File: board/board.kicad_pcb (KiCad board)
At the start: 2 copper layers, 50.8 x 22.9 mm, 17 parts, among them J1 MOTION DETECTOR, J2 EXT BUTTON, J3 GS2, J4 ~POWER, U3 ATTINY85

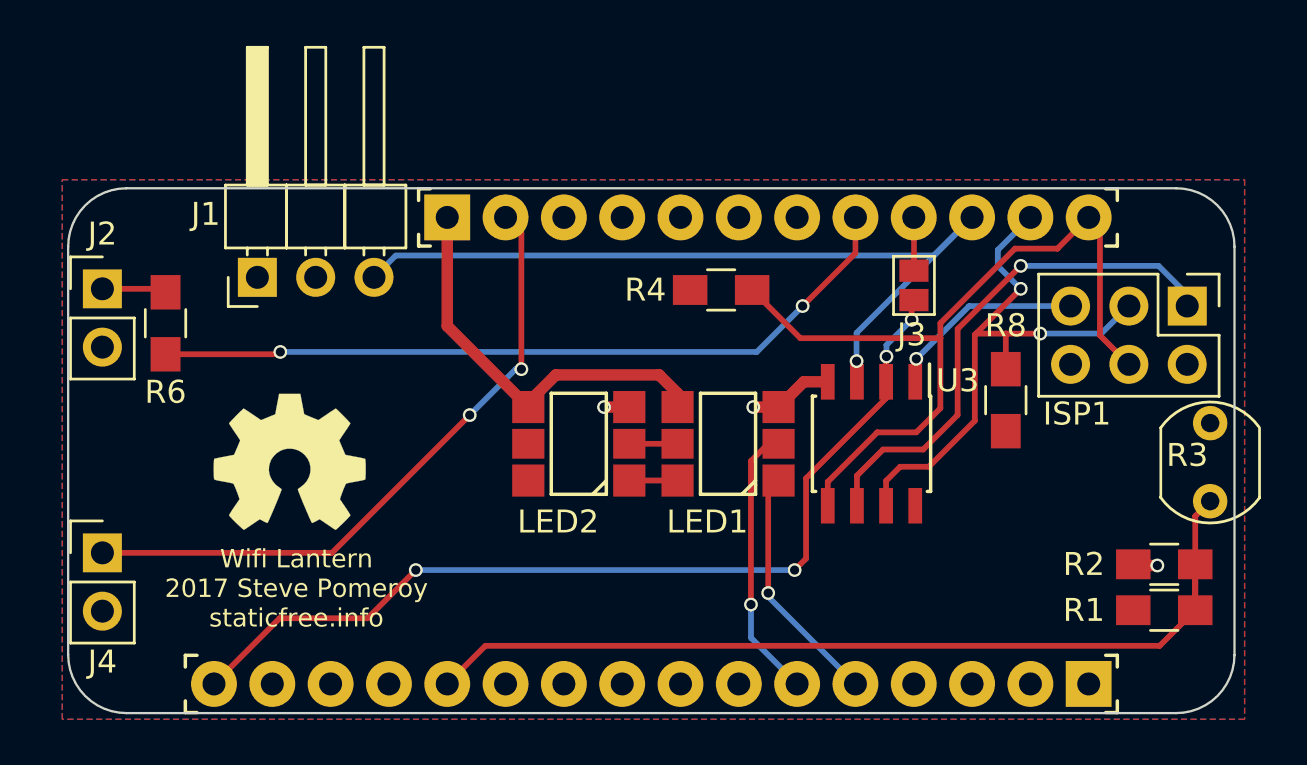
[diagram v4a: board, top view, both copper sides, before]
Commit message: Add power breakout; updated on-board docs
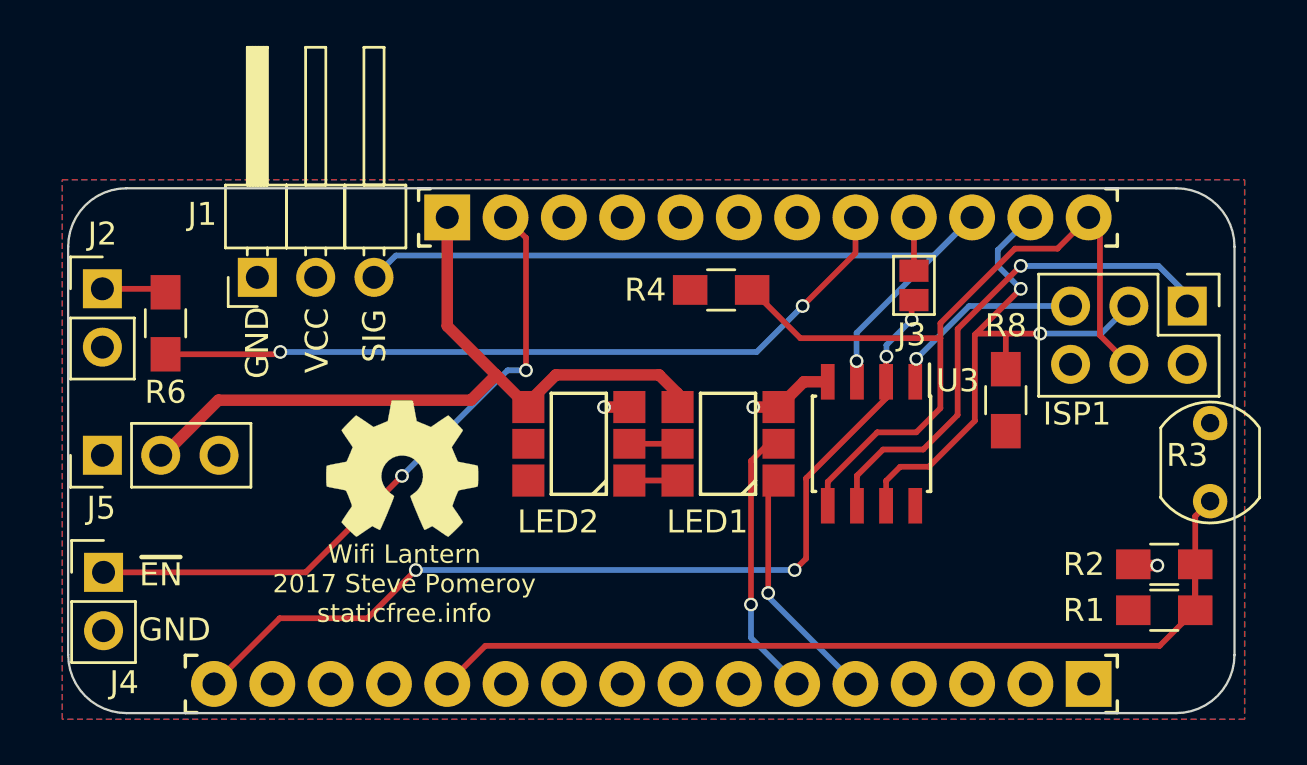
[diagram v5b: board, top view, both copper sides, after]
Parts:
- added J5: GPWR, Pin_Headers:Pin_Header_Straight_1x03_Pitch2.54mm, F.Cu at (113.2, 114.5)
- U3: value ATTINY85 -> ATTINY85-20PU
- moved REF*** 4.91 mm to (126.3, 115.1)
- moved J4 0.85 mm to (113.3, 119.6)
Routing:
- net /VBAT: track 18.1 -> 34.1 mm
- net /EN: track 28.5 -> 29.1 mm
- net Net-(ISP1-Pad5): vias 2 -> 1
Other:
- board text added: "EXT BTN (D9)"
- board text added: "GND"
- board text added: "J3: short for ESP8266 built-in RTC reset"
- board text added: "Power"
- board text added: "SIG"
- board text added: "VBAT"
- board text added: "VCC"
- board text added: "~EN"
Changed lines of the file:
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@@
 (kicad_pcb (version 4) (host pcbnew 4.0.6+dfsg1-1)
   (general
-    (links 40)
+    (links 43)
     (no_connects 0)
     (area 111.709999 102.819999 162.610001 125.780001)
     (thickness 1.6)
-    (drawings 9)
-    (tracks 140)
+    (drawings 20)
+    (tracks 144)
     (zones 0)
-    (modules 17)
+    (modules 18)
     (nets 19)
   )
@@
   )
   (module Pin_Headers:Pin_Header_Straight_1x02_Pitch2.54mm (layer F.Cu)
-    (at 113.25 118.75)
+    (at 113.3 119.6)
     (descr "Through hole straight pin header, 1x02, 2.54mm pitch, single row")
     (tags "Through hole pin header THT 1x02 2.54mm single row")
-    (fp_text reference J4 (at 0 4.75) (layer F.SilkS)
+    (fp_text reference J4 (at 0.9 4.8) (layer F.SilkS)
       (effects (font (size 1 1) (thickness 0.15)))
     )
@@
       (effects (font (size 1 1) (thickness 0.15)))
     )
-    (fp_text value ATTINY85 (at 3 0 360) (layer F.Fab)
+    (fp_text value ATTINY85-20PU (at 3 0 360) (layer F.Fab)
       (effects (font (size 1 1) (thickness 0.15)))
     )
@@
     (descr "Through hole angled pin header, 1x03, 2.54mm pitch, 6mm pin length, single row")
     (tags "Through hole angled pin header THT 1x03 2.54mm single row")
-    (fp_text reference J1 (at 2.75 -2.25 180) (layer F.SilkS)
+    (fp_text reference J1 (at 2.75 -2.4 180) (layer F.SilkS)
       (effects (font (size 1 1) (thickness 0.15)))
     )
@@
   )
   (module Symbols:OSHW-Symbol_6.7x6mm_SilkScreen (layer F.Cu)
-    (at 121.4 114.8)
+    (at 126.3 115.1)
     (descr "Open Source Hardware Symbol")
     (tags "Logo Symbol OSHW")
@@
       (xy 0.555814 -2.531069)) (layer F.SilkS) (width 0.01))
   )
-  (gr_text "Wifi Lantern\n2017 Steve Pomeroy\nstaticfree.info" (at 121.7 120.3) (layer F.SilkS)
+  (module Pin_Headers:Pin_Header_Straight_1x03_Pitch2.54mm (layer F.Cu)
+    (at 113.25 114.5 90)
+    (descr "Through hole straight pin header, 1x03, 2.54mm pitch, single row")
+    (tags "Through hole pin header THT 1x03 2.54mm single row")
+    (fp_text reference J5 (at -2.3 -0.05 180) (layer F.SilkS)
+      (effects (font (size 1 1) (thickness 0.15)))
+    )
+    (fp_text value GPWR (at 0 7.47 90) (layer F.Fab)
+      (effects (font (size 1 1) (thickness 0.15)))
+    )
+    (fp_line (start -1.27 -1.27) (end -1.27 6.35) (layer F.Fab) (width 0.1))
+    (fp_line (start -1.27 6.35) (end 1.27 6.35) (layer F.Fab) (width 0.1))
+    (fp_line (start 1.27 6.35) (end 1.27 -1.27) (layer F.Fab) (width 0.1))
+    (fp_line (start 1.27 -1.27) (end -1.27 -1.27) (layer F.Fab) (width 0.1))
+    (fp_line (start -1.39 1.27) (end -1.39 6.47) (layer F.SilkS) (width 0.12))
+    (fp_line (start -1.39 6.47) (end 1.39 6.47) (layer F.SilkS) (width 0.12))
+    (fp_line (start 1.39 6.47) (end 1.39 1.27) (layer F.SilkS) (width 0.12))
+    (fp_line (start 1.39 1.27) (end -1.39 1.27) (layer F.SilkS) (width 0.12))
+    (fp_line (start -1.39 0) (end -1.39 -1.39) (layer F.SilkS) (width 0.12))
+    (fp_line (start -1.39 -1.39) (end 0 -1.39) (layer F.SilkS) (width 0.12))
+    (fp_line (start -1.6 -1.6) (end -1.6 6.6) (layer F.CrtYd) (width 0.05))
+    (fp_line (start -1.6 6.6) (end 1.6 6.6) (layer F.CrtYd) (width 0.05))
+    (fp_line (start 1.6 6.6) (end 1.6 -1.6) (layer F.CrtYd) (width 0.05))
+    (fp_line (start 1.6 -1.6) (end -1.6 -1.6) (layer F.CrtYd) (width 0.05))
+    (pad 1 thru_hole rect (at 0 0 90) (size 1.7 1.7) (drill 1) (layers *.Cu *.Mask)
+      (net 5 VCC))
+    (pad 2 thru_hole oval (at 0 2.54 90) (size 1.7 1.7) (drill 1) (layers *.Cu *.Mask)
+      (net 4 /VBAT))
+    (pad 3 thru_hole oval (at 0 5.08 90) (size 1.7 1.7) (drill 1) (layers *.Cu *.Mask)
+      (net 3 GND))
+    (model Pin_Headers.3dshapes/Pin_Header_Straight_1x03_Pitch2.54mm.wrl
+      (at (xyz 0 -0.1 0))
+      (scale (xyz 1 1 1))
+      (rotate (xyz 0 0 90))
+    )
+  )
+  (gr_text VBAT (at 115.9 117.5 270) (layer B.SilkS)
+    (effects (font (size 1 1) (thickness 0.2)) (justify mirror))
+  )
+  (gr_text VCC (at 113.4 117.2 270) (layer B.SilkS)
+    (effects (font (size 1 1) (thickness 0.2)) (justify mirror))
+  )
+  (gr_text GND (at 118.4 117.4 270) (layer B.SilkS)
+    (effects (font (size 1 1) (thickness 0.2)) (justify mirror))
+  )
+  (gr_text Power (at 115.4 122 270) (layer B.SilkS)
+    (effects (font (size 0.7 0.7) (thickness 0.1)) (justify mirror))
+  )
+  (gr_text GND (at 116.4 122.1) (layer F.SilkS)
+    (effects (font (size 1 1) (thickness 0.2)))
+  )
+  (gr_text ~EN (at 115.8 119.7) (layer F.SilkS)
+    (effects (font (size 1 1) (thickness 0.2)))
+  )
+  (gr_text "EXT BTN (D9)" (at 115.2 108.5 270) (layer B.SilkS)
+    (effects (font (size 0.7 0.7) (thickness 0.1)) (justify mirror))
+  )
+  (gr_text SIG (at 125.1 109.3 90) (layer F.SilkS)
+    (effects (font (size 1 1) (thickness 0.2)))
+  )
+  (gr_text VCC (at 122.6 109.5 90) (layer F.SilkS)
+    (effects (font (size 1 1) (thickness 0.2)))
+  )
+  (gr_text GND (at 120 109.6 90) (layer F.SilkS)
+    (effects (font (size 1 1) (thickness 0.2)))
+  )
+  (gr_text "J3: short for\nESP8266 built-in RTC reset" (at 145.7 113.3) (layer B.SilkS)
+    (effects (font (size 0.7 0.7) (thickness 0.1)) (justify mirror))
+  )
+  (gr_text "Wifi Lantern\n2017 Steve Pomeroy\nstaticfree.info" (at 126.4 120.1) (layer F.SilkS)
     (effects (font (size 0.8 0.8) (thickness 0.1)))
   )
@@
   (segment (start 143.8 111.3) (end 144.845 111.3) (width 0.5) (layer F.Cu) (net 3) (status 20))
   (segment (start 136.2 112.4) (end 136.1 112.5) (width 0.5) (layer F.Cu) (net 3) (status 30))
+  (segment (start 115.79 114.5) (end 115.9 114.5) (width 0.5) (layer F.Cu) (net 4) (status 30))
+  (segment (start 115.9 114.5) (end 118.3 112.1) (width 0.5) (layer F.Cu) (net 4) (status 10))
+  (segment (start 118.3 112.1) (end 129.3 112.1) (width 0.5) (layer F.Cu) (net 4))
+  (segment (start 129.3 112.1) (end 130.4 111) (width 0.5) (layer F.Cu) (net 4))
   (segment (start 138.3 112.4) (end 138.3 112.2) (width 0.5) (layer F.Cu) (net 4) (status 30))
   (segment (start 131.8 112.4) (end 131.8 112.2) (width 0.5) (layer F.Cu) (net 4) (status 30))
@@
   (segment (start 133 111) (end 137.5 111) (width 0.5) (layer F.Cu) (net 4))
   (segment (start 138.3 111.8) (end 138.3 112.4) (width 0.5) (layer F.Cu) (net 4) (status 30))
-  (segment (start 131.8 112.4) (end 128.27 108.87) (width 0.5) (layer F.Cu) (net 4) (status 10))
+  (segment (start 131.8 112.4) (end 130.4 111) (width 0.5) (layer F.Cu) (net 4) (status 10))
+  (segment (start 130.4 111) (end 128.27 108.87) (width 0.5) (layer F.Cu) (net 4))
   (segment (start 128.27 108.87) (end 128.27 104.14) (width 0.5) (layer F.Cu) (net 4) (status 20))
   (segment (start 120.65 124.35) (end 120.65 124.46) (width 0.5) (layer F.Cu) (net 5) (status 30))
@@
   (via (at 148.7 110.3) (size 0.6) (drill 0.4) (layers F.Cu B.Cu) (net 10))
   (segment (start 151 108) (end 148.7 110.3) (width 0.25) (layer B.Cu) (net 10))
-  (via (at 155.42 108) (size 0.6) (drill 0.4) (layers F.Cu B.Cu) (net 10) (status 30))
   (segment (start 148.7 111.255) (end 148.655 111.3) (width 0.25) (layer F.Cu) (net 10) (status 30))
   (segment (start 116 107.4) (end 115.85 107.25) (width 0.25) (layer F.Cu) (net 11) (status 30))
@@
   (segment (start 148 115) (end 149.25 115) (width 0.25) (layer F.Cu) (net 15))
   (segment (start 147.385 115.615) (end 148 115) (width 0.25) (layer F.Cu) (net 15))
-  (segment (start 144.845 116.7) (end 144.845 115.655) (width 0.25) (layer F.Cu) (net 16))
+  (segment (start 144.845 116.7) (end 144.845 115.655) (width 0.25) (layer F.Cu) (net 16) (status 10))
   (segment (start 149.75 112.45) (end 149.75 109.4) (width 0.25) (layer F.Cu) (net 16))
   (segment (start 148.7 113.5) (end 149.75 112.45) (width 0.25) (layer F.Cu) (net 16))
@@
   (segment (start 149.75 108.75) (end 153 105.5) (width 0.25) (layer F.Cu) (net 16))
   (segment (start 149.75 109.4) (end 149.75 108.75) (width 0.25) (layer F.Cu) (net 16))
-  (segment (start 113.25 118.75) (end 123.25 118.75) (width 0.25) (layer F.Cu) (net 17) (status 10))
-  (segment (start 131.5 110.75) (end 131.5 104.83) (width 0.25) (layer F.Cu) (net 17) (status 20))
-  (via (at 131.5 110.75) (size 0.6) (drill 0.4) (layers F.Cu B.Cu) (net 17))
-  (segment (start 131.25 110.75) (end 131.5 110.75) (width 0.25) (layer B.Cu) (net 17))
-  (segment (start 129.25 112.75) (end 131.25 110.75) (width 0.25) (layer B.Cu) (net 17))
-  (via (at 129.25 112.75) (size 0.6) (drill 0.4) (layers F.Cu B.Cu) (net 17))
-  (segment (start 123.25 118.75) (end 129.25 112.75) (width 0.25) (layer F.Cu) (net 17))
-  (segment (start 131.5 104.83) (end 130.81 104.14) (width 0.25) (layer F.Cu) (net 17) (status 30))
+  (segment (start 113.3 119.6) (end 122.1 119.6) (width 0.25) (layer F.Cu) (net 17) (status 10))
+  (segment (start 131.7 105.03) (end 130.81 104.14) (width 0.25) (layer F.Cu) (net 17) (status 20))
+  (segment (start 131.7 110.8) (end 131.7 105.03) (width 0.25) (layer F.Cu) (net 17))
+  (via (at 131.7 110.8) (size 0.6) (drill 0.4) (layers F.Cu B.Cu) (net 17))
+  (segment (start 130.9 110.8) (end 131.7 110.8) (width 0.25) (layer B.Cu) (net 17))
+  (segment (start 126.3 115.4) (end 130.9 110.8) (width 0.25) (layer B.Cu) (net 17))
+  (via (at 126.3 115.4) (size 0.6) (drill 0.4) (layers F.Cu B.Cu) (net 17))
+  (segment (start 122.1 119.6) (end 126.3 115.4) (width 0.25) (layer F.Cu) (net 17))
   (segment (start 116 110.1) (end 120.9 110.1) (width 0.25) (layer F.Cu) (net 18) (status 10))
   (segment (start 146.05 105.7) (end 146.05 104.14) (width 0.25) (layer F.Cu) (net 18) (status 20))

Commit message: Improve on-board docs
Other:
- board text added: "EXT BTN"
- board text added: "Wifi Lantern v0.5.0 2017 Steve Pomeroy staticfree.info"
- board text added: "~Power"
- board text removed: "EXT BTN (D9)"
- board text removed: "Power"
- board text removed: "Wifi Lantern 2017 Steve Pomeroy staticfree.info"
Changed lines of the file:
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@@
     (descr "Through hole straight pin header, 1x02, 2.54mm pitch, single row")
     (tags "Through hole pin header THT 1x02 2.54mm single row")
-    (fp_text reference J4 (at 0.9 4.8) (layer F.SilkS)
-      (effects (font (size 1 1) (thickness 0.15)))
+    (fp_text reference J4 (at 0.9 4.8) (layer B.SilkS)
+      (effects (font (size 1 1) (thickness 0.15)) (justify mirror))
     )
     (fp_text value ~POWER (at -4.5 1 180) (layer F.Fab)
@@
     (tags "solder bridge")
     (attr smd)
-    (fp_text reference J3 (at -0.1 2.15 180) (layer F.SilkS)
+    (fp_text reference J3 (at -2 -0.7 180) (layer F.SilkS)
       (effects (font (size 1 1) (thickness 0.15)))
     )
@@
     (tags "resistor 0805")
     (attr smd)
-    (fp_text reference R8 (at 3.25 0 180) (layer F.SilkS)
+    (fp_text reference R8 (at 3 0 180) (layer F.SilkS)
       (effects (font (size 1 1) (thickness 0.15)))
     )
@@
       (effects (font (size 1 1) (thickness 0.15)))
     )
-    (fp_text user %R (at 3.25 0 180) (layer F.Fab)
+    (fp_text user %R (at 3 0 180) (layer F.Fab)
       (effects (font (size 1 1) (thickness 0.15)))
     )
@@
       (effects (font (size 1 1) (thickness 0.15)))
     )
-    (fp_text user %R (at -3.2 0 180) (layer F.Fab)
+    (fp_text user %R (at -3.3 0 180) (layer F.Fab)
       (effects (font (size 1 1) (thickness 0.15)))
     )
@@
     (descr "Through hole straight pin header, 1x02, 2.54mm pitch, single row")
     (tags "Through hole pin header THT 1x02 2.54mm single row")
-    (fp_text reference J2 (at 0 -2.39) (layer F.SilkS)
-      (effects (font (size 1 1) (thickness 0.15)))
+    (fp_text reference J2 (at 0 -2.39) (layer B.SilkS)
+      (effects (font (size 1 1) (thickness 0.15)) (justify mirror))
     )
     (fp_text value "EXT BUTTON" (at -6.25 1.5) (layer F.Fab)
@@
     (tags "SOIC 1.27")
     (attr smd)
-    (fp_text reference U3 (at -2.75 -3.75 360) (layer F.SilkS)
+    (fp_text reference U3 (at -4.3 1.75 360) (layer F.SilkS)
       (effects (font (size 1 1) (thickness 0.15)))
     )
@@
     (descr "Resistor, LDR 5.1x3.4mm")
     (tags "Resistor LDR5.1x3.4mm")
-    (fp_text reference R3 (at 2 -1 180) (layer F.SilkS)
+    (fp_text reference R3 (at 1.7 -1 180) (layer F.SilkS)
       (effects (font (size 1 1) (thickness 0.15)))
     )
@@
     (descr "Through hole straight pin header, 1x03, 2.54mm pitch, single row")
     (tags "Through hole pin header THT 1x03 2.54mm single row")
-    (fp_text reference J5 (at -2.3 -0.05 180) (layer F.SilkS)
-      (effects (font (size 1 1) (thickness 0.15)))
+    (fp_text reference J5 (at -2.3 -0.05 180) (layer B.SilkS)
+      (effects (font (size 1 1) (thickness 0.15)) (justify mirror))
     )
     (fp_text value GPWR (at 0 7.47 90) (layer F.Fab)
@@
     )
   )
-  (gr_text VBAT (at 115.9 117.5 270) (layer B.SilkS)
-    (effects (font (size 1 1) (thickness 0.2)) (justify mirror))
-  )
-  (gr_text VCC (at 113.4 117.2 270) (layer B.SilkS)
-    (effects (font (size 1 1) (thickness 0.2)) (justify mirror))
-  )
-  (gr_text GND (at 118.4 117.4 270) (layer B.SilkS)
-    (effects (font (size 1 1) (thickness 0.2)) (justify mirror))
-  )
-  (gr_text Power (at 115.4 122 270) (layer B.SilkS)
-    (effects (font (size 0.7 0.7) (thickness 0.1)) (justify mirror))
-  )
-  (gr_text GND (at 116.4 122.1) (layer F.SilkS)
-    (effects (font (size 1 1) (thickness 0.2)))
-  )
-  (gr_text ~EN (at 115.8 119.7) (layer F.SilkS)
-    (effects (font (size 1 1) (thickness 0.2)))
-  )
-  (gr_text "EXT BTN (D9)" (at 115.2 108.5 270) (layer B.SilkS)
-    (effects (font (size 0.7 0.7) (thickness 0.1)) (justify mirror))
-  )
-  (gr_text SIG (at 125.1 109.3 90) (layer F.SilkS)
-    (effects (font (size 1 1) (thickness 0.2)))
-  )
-  (gr_text VCC (at 122.6 109.5 90) (layer F.SilkS)
-    (effects (font (size 1 1) (thickness 0.2)))
-  )
-  (gr_text GND (at 120 109.6 90) (layer F.SilkS)
-    (effects (font (size 1 1) (thickness 0.2)))
+  (gr_text VBAT (at 115.8 117.3 90) (layer F.SilkS)
+    (effects (font (size 0.7 0.7) (thickness 0.1)))
+  )
+  (gr_text VCC (at 113.3 117.1 90) (layer F.SilkS)
+    (effects (font (size 0.7 0.7) (thickness 0.1)))
+  )
+  (gr_text GND (at 118.4 117.1 90) (layer F.SilkS)
+    (effects (font (size 0.7 0.7) (thickness 0.1)))
+  )
+  (gr_text ~Power (at 114.3 124.4) (layer F.SilkS)
+    (effects (font (size 0.8 0.8) (thickness 0.1)))
+  )
+  (gr_text GND (at 116 122.2) (layer F.SilkS)
+    (effects (font (size 0.7 0.7) (thickness 0.1)))
+  )
+  (gr_text ~EN (at 115.7 119.6) (layer F.SilkS)
+    (effects (font (size 0.7 0.7) (thickness 0.1)))
+  )
+  (gr_text "EXT BTN" (at 114.4 105.2) (layer F.SilkS)
+    (effects (font (size 0.7 0.7) (thickness 0.1)))
+  )
+  (gr_text SIG (at 125.1 109.2 90) (layer F.SilkS)
+    (effects (font (size 0.7 0.7) (thickness 0.1)))
+  )
+  (gr_text VCC (at 122.6 109.4 90) (layer F.SilkS)
+    (effects (font (size 0.7 0.7) (thickness 0.1)))
+  )
+  (gr_text GND (at 120 109.5 90) (layer F.SilkS)
+    (effects (font (size 0.7 0.7) (thickness 0.1)))
   )
   (gr_text "J3: short for\nESP8266 built-in RTC reset" (at 145.7 113.3) (layer B.SilkS)
     (effects (font (size 0.7 0.7) (thickness 0.1)) (justify mirror))
   )
-  (gr_text "Wifi Lantern\n2017 Steve Pomeroy\nstaticfree.info" (at 126.4 120.1) (layer F.SilkS)
+  (gr_text "Wifi Lantern v0.5.0\n2017 Steve Pomeroy\nstaticfree.info" (at 126.3 120.1) (layer F.SilkS)
     (effects (font (size 0.8 0.8) (thickness 0.1)))
   )
